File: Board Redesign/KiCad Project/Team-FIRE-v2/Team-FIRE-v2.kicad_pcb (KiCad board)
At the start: 4 copper layers, 95.2 x 88.9 mm, 0 parts

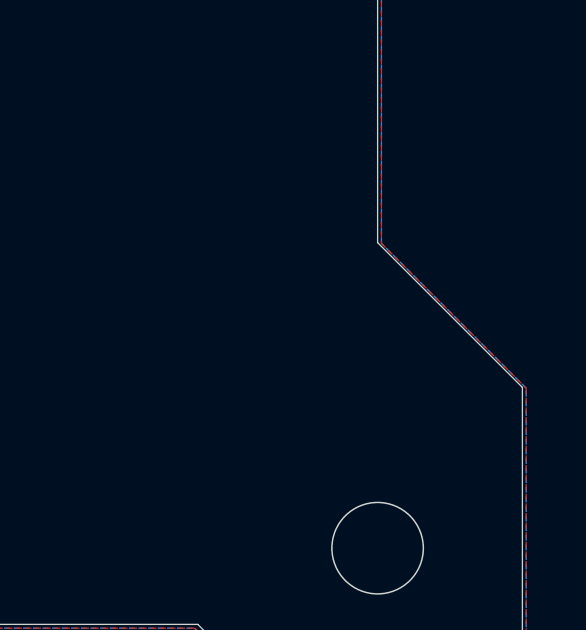
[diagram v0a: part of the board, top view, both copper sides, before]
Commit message: Replaced transistor symbol, and footprint
- Had to replace the CSD18543Q3AT transistor with a custom symbol, footprint and 3D model to account for the 9-pin package it resides in (not a 3 pin as the symbol depicts)
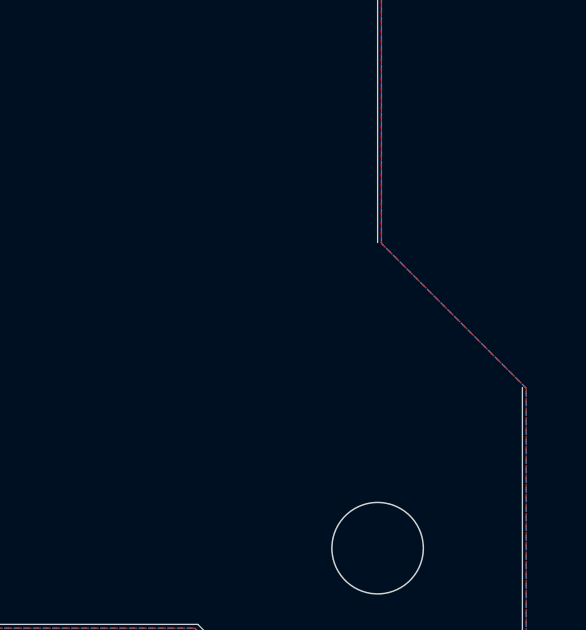
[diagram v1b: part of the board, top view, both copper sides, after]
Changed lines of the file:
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@@
   (general
     (thickness 1.6)
-    (drawings 25)
+    (drawings 24)
     (tracks 0)
     (zones 0)
@@
   (gr_line (start 120.65 114.3) (end 120.65 101.9556) (layer Edge.Cuts) (width 0.0254))
   (gr_line (start 120.65 37.7444) (end 120.65 25.4) (layer Edge.Cuts) (width 0.0254))
-  (gr_line (start 115.824 97.1296) (end 120.65 101.9556) (layer Edge.Cuts) (width 0.0254))
   (gr_line (start 115.824 42.5704) (end 115.824 97.1296) (layer Edge.Cuts) (width 0.0254))
   (gr_line (start 115.824 42.5704) (end 120.65 37.7444) (layer Edge.Cuts) (width 0.0254))

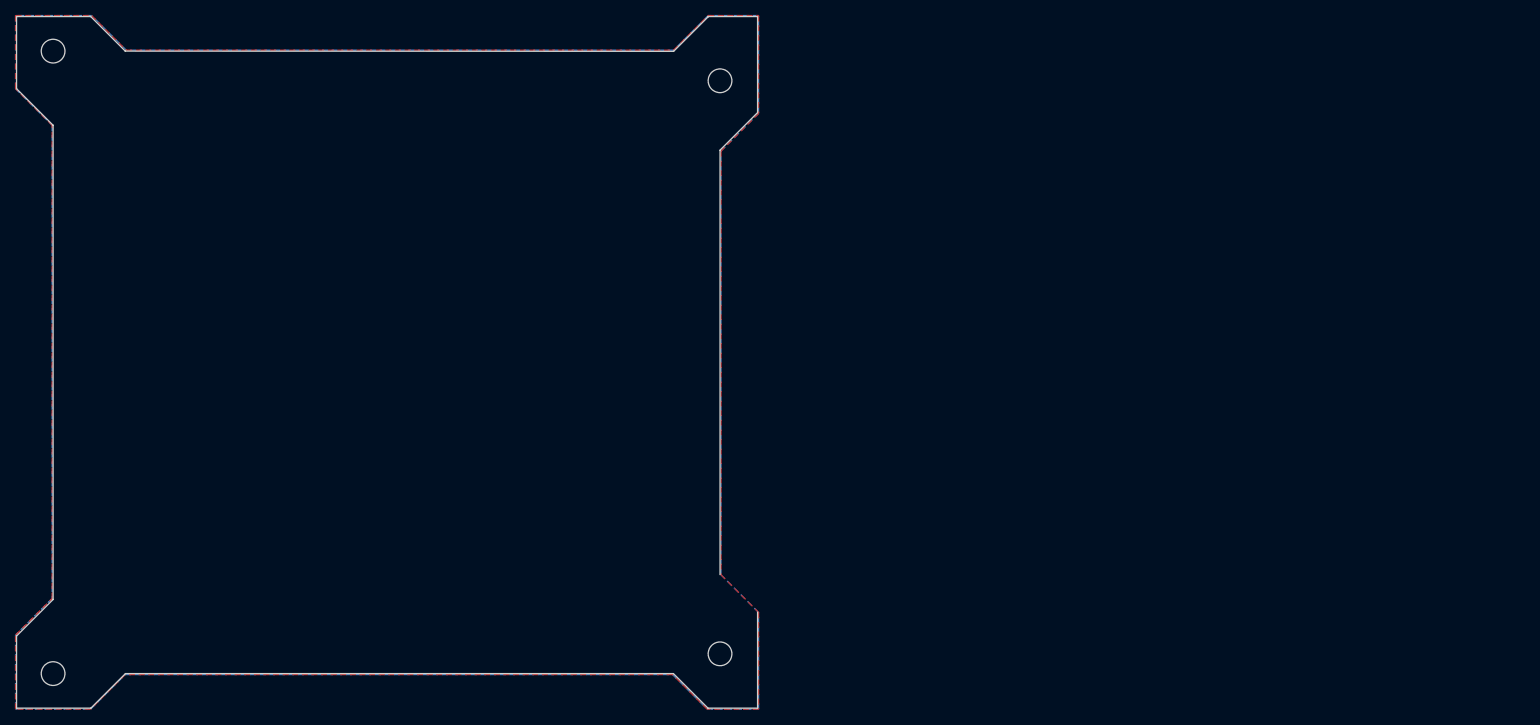
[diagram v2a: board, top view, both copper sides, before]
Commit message: Did some preliminary PCB work
- Started the PCB layout
- Put connectors in their probable spots
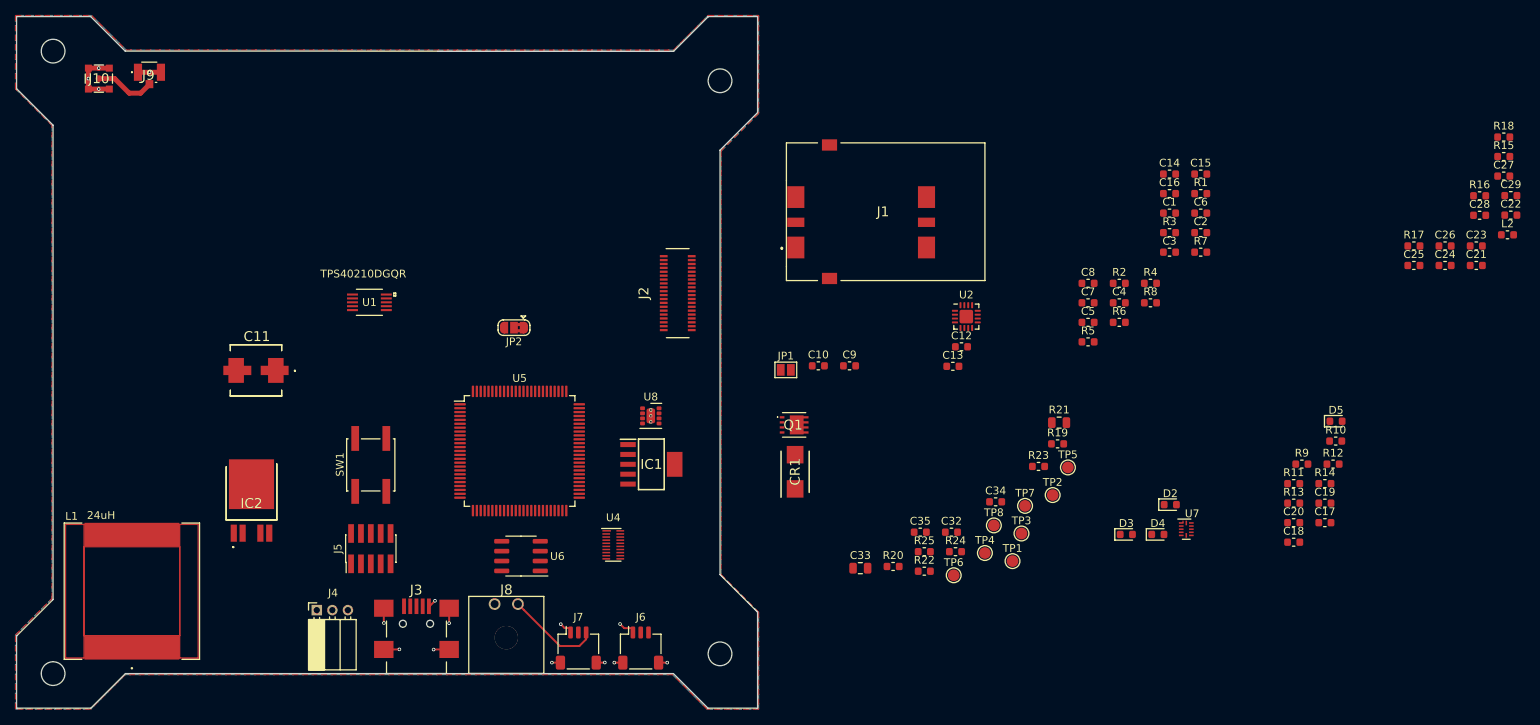
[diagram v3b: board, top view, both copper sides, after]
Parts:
- added C1: 33nF, Capacitor_SMD:C_0603_1608Metric, F.Cu at (173.6, 50.7)
- added C10: 470nF, Capacitor_SMD:C_0603_1608Metric, F.Cu at (128.5, 70.3)
- added C11: 39uF, Team-FIRE:EEEFK1H390SV, F.Cu at (56.2, 70.9)
- added C12: 1uF, Capacitor_SMD:C_0603_1608Metric, F.Cu at (146.9, 67.8)
- added C13: 2.2uF, Capacitor_SMD:C_0603_1608Metric, F.Cu at (145.8, 70.4)
- added C14: 10uF, Capacitor_SMD:C_0603_1608Metric, F.Cu at (173.6, 45.6)
- added C15: 0.1uF, Capacitor_SMD:C_0603_1608Metric, F.Cu at (177.6, 45.6)
- added C16: 0.1uF, Capacitor_SMD:C_0603_1608Metric, F.Cu at (173.6, 48.2)
- added C17: 0.1uF, Capacitor_SMD:C_0603_1608Metric, F.Cu at (193.6, 90.5)
- added C18: 0.1uF, Capacitor_SMD:C_0603_1608Metric, F.Cu at (189.6, 93.0)
- added C19: 0.1uF, Capacitor_SMD:C_0603_1608Metric, F.Cu at (193.6, 87.9)
- added C2: 100pF, Capacitor_SMD:C_0603_1608Metric, F.Cu at (177.6, 53.2)
- added C20: 0.1uF, Capacitor_SMD:C_0603_1608Metric, F.Cu at (189.6, 90.5)
- added C21: 10uF, Capacitor_SMD:C_0603_1608Metric, F.Cu at (213.0, 57.4)
- added C22: 10uF, Capacitor_SMD:C_0603_1608Metric, F.Cu at (217.5, 50.9)
- added C23: 10uF, Capacitor_SMD:C_0603_1608Metric, F.Cu at (213.0, 54.9)
- added C24: 10uF, Capacitor_SMD:C_0603_1608Metric, F.Cu at (209.0, 57.4)
- added C25: 10uF, Capacitor_SMD:C_0603_1608Metric, F.Cu at (205.0, 57.4)
- added C26: 100nF, Capacitor_SMD:C_0603_1608Metric, F.Cu at (209.0, 54.9)
- added C27: 4.7uF, Capacitor_SMD:C_0603_1608Metric, F.Cu at (216.6, 45.9)
- added C28: 100nF, Capacitor_SMD:C_0603_1608Metric, F.Cu at (213.5, 50.9)
- added C29: 100nF, Capacitor_SMD:C_0603_1608Metric, F.Cu at (217.5, 48.4)
- added C3: 1.5nF, Capacitor_SMD:C_0603_1608Metric, F.Cu at (173.6, 55.7)
- added C32: 10uF, Capacitor_SMD:C_0603_1608Metric, F.Cu at (145.6, 91.7)
- added C33: 47uF, Capacitor_SMD:C_0805_2012Metric, F.Cu at (133.9, 96.3)
- added C34: 430pF, Capacitor_SMD:C_0603_1608Metric, F.Cu at (151.3, 87.8)
- added C35: 1uF, Capacitor_SMD:C_0603_1608Metric, F.Cu at (141.6, 91.7)
- added C4: 27nF, Capacitor_SMD:C_0603_1608Metric, F.Cu at (167.1, 62.2)
- added C5: 0.1u, Capacitor_SMD:C_0603_1608Metric, F.Cu at (163.1, 64.7)
- added C6: 1uF, Capacitor_SMD:C_0603_1608Metric, F.Cu at (177.6, 50.7)
- added C7: 150pF, Capacitor_SMD:C_0603_1608Metric, F.Cu at (163.1, 62.2)
- added C8: 1uF, Capacitor_SMD:C_0603_1608Metric, F.Cu at (163.1, 59.7)
- added C9: 10uF, Capacitor_SMD:C_0603_1608Metric, F.Cu at (132.5, 70.3)
- added CR1: B260-13-F, Team-FIRE:DIOM5336X250N, F.Cu at (125.5, 83.9)
- added D2: Blue, LED_SMD:LED_0603_1608Metric, F.Cu at (173.7, 88.1)
- added D3: Green, LED_SMD:LED_0603_1608Metric, F.Cu at (168.1, 92.0)
- added D4: Orange, LED_SMD:LED_0603_1608Metric, F.Cu at (172.1, 92.0)
- added D5: Yellow, LED_SMD:LED_0603_1608Metric, F.Cu at (195.0, 77.4)
- added IC1: MCP1826T-3302E_DC, Team-FIRE:SOT127P706X180-6N, F.Cu at (107.0, 83.0)
- added IC2: BTS500601TEAAUMA2, Team-FIRE:BTS500601TEAAUMA2, F.Cu at (55.6, 86.5)
- added J1: 47388-2001, Team-FIRE:473882001, F.Cu at (136.8, 50.5)
- added J10: PCB.MMCX.F.ST.SMT.JACK.HT, Team-FIRE:PCBMMCXFSTSMTJACKHT, F.Cu at (36.0, 33.4)
- added J2: 53885-0408, Team-FIRE:538850408, F.Cu at (110.4, 61.0)
- added J3: UX60-MB-5ST, Team-FIRE:HIROSE-UX60-MB-5ST, F.Cu at (76.8, 101.2)
- added J4: Conn_01x03, Connector_PinSocket_2.00mm:PinSocket_1x03_P2.00mm_Horizontal, F.Cu at (64.0, 101.7)
- added J5: Conn_ARM_JTAG_SWD_10, Connector_PinHeader_1.27mm:PinHeader_2x05_P1.27mm_Vertical_SMD, F.Cu at (70.9, 93.8)
- added J6: Conn_01x03, Connector_JST:JST_SH_SM03B-SRSS-TB_1x03-1MP_P1.00mm_Horizontal, F.Cu at (105.6, 106.6)
- added J7: Conn_01x03, Connector_JST:JST_SH_SM03B-SRSS-TB_1x03-1MP_P1.00mm_Horizontal, F.Cu at (97.6, 106.6)
- added J8: Conn_01x02, Team-FIRE:43650-0200, F.Cu at (89.9, 100.9)
- added J9: U.FL-R-SMT_10_, Team-FIRE:UFLRSMT10, F.Cu at (42.5, 32.6)
- added JP1: SolderJumper_2_Open, Jumper:SolderJumper-2_P1.3mm_Open_Pad1.0x1.5mm, F.Cu at (124.3, 70.8)
- added JP2: SolderJumper_3_Bridged12, Jumper:SolderJumper-3_P1.3mm_Bridged2Bar12_RoundedPad1.0x1.5mm, F.Cu at (89.3, 65.4)
- added L1: 24uH, Team-FIRE:IHLP6767GZER220M11, F.Cu at (40.2, 99.3)
- added L2: 10uH, Inductor_SMD:L_0603_1608Metric, F.Cu at (217.0, 53.5)
- added Q1: CSD18543Q3AT, Team-FIRE:CSD18543Q3AT, F.Cu at (125.0, 77.9)
- added R1: 12.1k, Resistor_SMD:R_0603_1608Metric, F.Cu at (177.6, 48.2)
- added R10: 10k, Resistor_SMD:R_0603_1608Metric, F.Cu at (195.0, 80.0)
- added R11: 330, Resistor_SMD:R_0603_1608Metric, F.Cu at (189.6, 85.4)
- added R12: 330, Resistor_SMD:R_0603_1608Metric, F.Cu at (194.6, 82.9)
- added R13: 330, Resistor_SMD:R_0603_1608Metric, F.Cu at (189.6, 87.9)
- added R14: 330, Resistor_SMD:R_0603_1608Metric, F.Cu at (193.6, 85.4)
- added R15: 10k, Resistor_SMD:R_0603_1608Metric, F.Cu at (216.6, 43.4)
- added R16: 10k, Resistor_SMD:R_0603_1608Metric, F.Cu at (213.5, 48.4)
- added R17: 330, Resistor_SMD:R_0603_1608Metric, F.Cu at (205.0, 54.9)
- added R18: 1k, Resistor_SMD:R_0603_1608Metric, F.Cu at (216.6, 40.9)
- added R19: 100k, Resistor_SMD:R_0603_1608Metric, F.Cu at (159.2, 80.3)
- added R2: 1.13k, Resistor_SMD:R_0603_1608Metric, F.Cu at (167.1, 59.7)
- added R20: 10k, Resistor_SMD:R_0603_1608Metric, F.Cu at (138.1, 96.1)
- added R21: 523k, Resistor_SMD:R_0805_2012Metric, F.Cu at (159.4, 77.6)
- added R22: 10k, Resistor_SMD:R_0603_1608Metric, F.Cu at (142.1, 96.7)
- added R23: 1k, Resistor_SMD:R_0603_1608Metric, F.Cu at (156.8, 83.2)
- added R24: 100k, Resistor_SMD:R_0603_1608Metric, F.Cu at (146.1, 94.2)
- added R25: 1k, Resistor_SMD:R_0603_1608Metric, F.Cu at (142.1, 94.2)
- added R3: 301k, Resistor_SMD:R_0603_1608Metric, F.Cu at (173.6, 53.2)
- added R4: 47.5k, Resistor_SMD:R_0603_1608Metric, F.Cu at (171.2, 59.7)
- added R5: 19.1, Resistor_SMD:R_0603_1608Metric, F.Cu at (163.1, 67.2)
- added R6: 1k, Resistor_SMD:R_0603_1608Metric, F.Cu at (167.1, 64.7)
- added R7: 15m, Resistor_SMD:R_0603_1608Metric, F.Cu at (177.6, 55.7)
- added R8: 100k, Resistor_SMD:R_0603_1608Metric, F.Cu at (171.2, 62.2)
- added R9: 10k, Resistor_SMD:R_0603_1608Metric, F.Cu at (190.6, 82.9)
- added SW1: RESET, Button_Switch_SMD:SW_SPST_EVQQ2, F.Cu at (70.9, 83.0)
- added TP1: TestPoint, TestPoint:TestPoint_Pad_D1.5mm, F.Cu at (153.4, 95.4)
- added TP2: TestPoint, TestPoint:TestPoint_Pad_D1.5mm, F.Cu at (158.6, 86.9)
- added TP3: TestPoint, TestPoint:TestPoint_Pad_D1.5mm, F.Cu at (154.6, 91.8)
- added TP4: TestPoint, TestPoint:TestPoint_Pad_D1.5mm, F.Cu at (149.9, 94.4)
- added TP5: TestPoint, TestPoint:TestPoint_Pad_D1.5mm, F.Cu at (160.5, 83.4)
- added TP6: TestPoint, TestPoint:TestPoint_Pad_D1.5mm, F.Cu at (145.9, 97.2)
- added TP7: TestPoint, TestPoint:TestPoint_Pad_D1.5mm, F.Cu at (155.0, 88.3)
- added TP8: TestPoint, TestPoint:TestPoint_Pad_D1.5mm, F.Cu at (151.0, 90.8)
- added U1: TPS40210DGQR, Team-FIRE:TPS40210DGQR, F.Cu at (70.8, 62.1)
- added U2: NCN4555MN, Package_DFN_QFN:QFN-16-1EP_3x3mm_P0.5mm_EP1.75x1.75mm, F.Cu at (147.5, 64.0)
- added U4: TXB0108DQSR, Package_SON:USON-20_2x4mm_P0.4mm, F.Cu at (102.1, 93.3)
- added U5: SAMD51, Package_QFP:TQFP-100_14x14mm_P0.5mm, F.Cu at (90.1, 81.2)
- added U6: AT25DF041B-SSHN-T, Package_SO:SOIC-8_3.9x4.9mm_P1.27mm, F.Cu at (90.2, 94.7)
- added U7: TXB0104RUT, Package_DFN_QFN:Texas_R_PUQFN-N12, F.Cu at (175.8, 91.3)
- added U8: TPS82140, Package_LGA:Texas_SIL0008D_MicroSiP-8-1EP_2.8x3mm_P0.65mm_EP1.1x1.9mm_ThermalVias, F.Cu at (106.9, 76.7)
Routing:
- net GND: track 0.00 -> 27.4 mm, vias 0 -> 15
- net TES-GPS-FLAG: track 0.00 -> 12.2 mm
- net Net-(J10-Pad1): track 0.00 -> 7.77 mm
- added copper zone on B.Cu, net (none)
- added copper zone on F.Cu, net (none)
- added copper zone on GND.Cu, net GND
- removed copper zone on B.Cu, net GND
- removed copper zone on F.Cu, net GND

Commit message: Finished PCB
- Added various 3D models for a complete 3D visualization of the PCB
- Generated a finalized netlist
- Fixed misnamed net from IR_SIM_RST to IR_SIM_RESET
- Finished all component placement for the PCB; the only work remaining are the mounting holes, and the grounding vias for the IRIDIUM
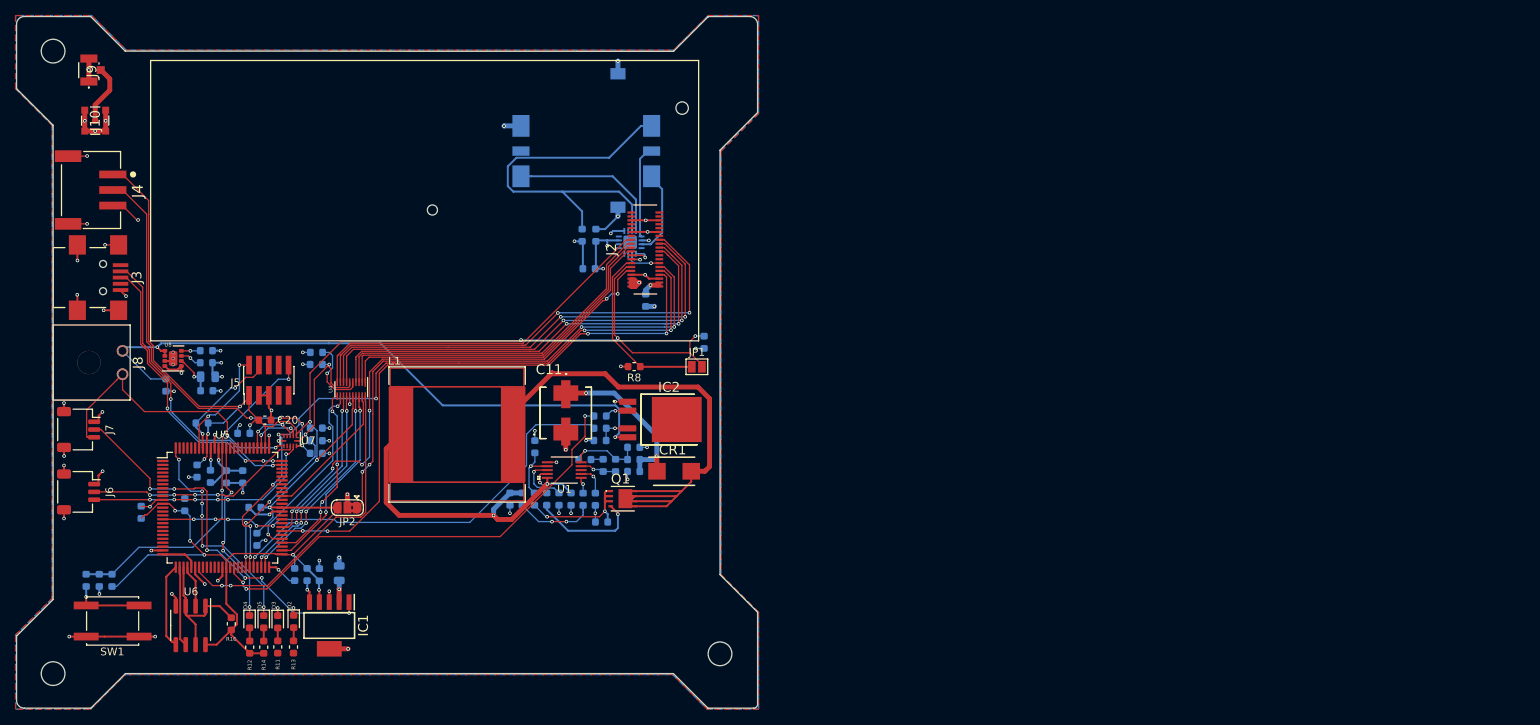
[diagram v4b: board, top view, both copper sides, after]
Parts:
- removed TP1, TP2, TP3, TP4, TP5, TP6, TP7, TP8: TestPoint, TestPoint:TestPoint_Pad_D1.5mm
- C1, C10, C12, C13, C14, C15, C16, C17, C18, C19, C2, C21, C22, C23, C24, C25, C26, C27, C28, C29, C3, C32, C33, C34, C35, C4, C5, C6, C7, C8, C9, J1, L2, R1, R10, R15, R17, R18, R19, R2, R20, R21, R22, R23, R24, R25, R3, R4, R5, R6, R7, R9, U2: moved to B.Cu
- J4: footprint Connector_PinSocket_2.00mm:PinSocket_1x03_P2.00mm_Horizontal -> Team-FIRE:JST_S3B-PH-SM4-TB(LF)(SN)
- moved C29 188.1 mm to (36.0, 97.9), turned to 270 degrees
- moved R15 187.0 mm to (37.7, 97.9), turned to 90 degrees
- moved R17 176.0 mm to (34.3, 97.9), turned to 90 degrees
- moved C21 174.5 mm to (41.4, 89.1), turned to 270 degrees
- moved R18 171.3 mm to (49.2, 77.6), turned to 180 degrees
- moved R16 169.6 mm to (53.0, 103.5), turned to 90 degrees
- moved L2 169.6 mm to (50.3, 84.5), turned to 90 degrees
- moved C27 166.6 mm to (54.5, 84.6), turned to 270 degrees
- moved C28 164.6 mm to (52.4, 84.6), turned to 270 degrees
- moved C22 163.0 mm to (61.1, 97.1), turned to 270 degrees
- moved C24 162.6 mm to (48.6, 83.8), turned to 270 degrees
- moved C23 161.2 mm to (56.3, 92.6), turned to 270 degrees
- moved C26 156.6 mm to (56.0, 88.5), turned to 180 degrees
- moved C25 152.0 mm to (54.6, 79.0), turned to 180 degrees
- moved R12 141.2 mm to (55.4, 106.5), turned to 270 degrees
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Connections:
- net IR_SIM_CLK renamed IR_SIM_CLOCK
- J2 pad 26: IR_SIM_RST -> IR_SIM_RESET
- J6 pad MP: GND -> (no net)
- J7 pad MP: GND -> (no net)
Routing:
- net MODE_SW: track 0.00 -> 261.4 mm, vias 0 -> 15
- net GND: track 27.4 -> 132.6 mm, vias 15 -> 67
- net TX_ACTIVE: track 0.00 -> 88.3 mm, vias 0 -> 7
- net VBAT: track 0.00 -> 82.1 mm, vias 0 -> 2
- net BOOST_EN: track 0.00 -> 77.9 mm, vias 0 -> 4
- net Net-(CR1-Pad2): track 0.00 -> 70.3 mm
- net 3.3V_SENSE: track 0.00 -> 68.3 mm, vias 0 -> 4
- net PWR_EN: track 0.00 -> 67.9 mm, vias 0 -> 6
- net 8V_ISENSE: track 0.00 -> 64.0 mm, vias 0 -> 5
- net RX: track 0.00 -> 62.0 mm, vias 0 -> 2
- net CTS: track 0.00 -> 60.6 mm, vias 0 -> 2
- net 8V_EN: track 0.00 -> 60.1 mm, vias 0 -> 3
- net DSR: track 0.00 -> 59.3 mm, vias 0 -> 2
- net RTS: track 0.00 -> 57.2 mm, vias 0 -> 2
- net Net-(C19-Pad2): track 0.00 -> 52.7 mm, vias 0 -> 4
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- added copper zone on PWR.Cu, net +5V
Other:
- board size 95.2 x 88.9 mm -> 95.3 x 88.9 mm
- net class Default: clearance 0.127 -> 0.075
- rule trace_clearance: 0.127 -> 0.075
